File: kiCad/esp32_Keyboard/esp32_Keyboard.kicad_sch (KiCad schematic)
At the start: 171 parts, among them SW1 Switch, SW10 Switch, SW11 Switch, SW12 Switch, SW13 Switch, SW14 Switch, SW15 Switch, SW16 Switch, SW17 Switch, SW18 Switch, SW19 Switch, SW2 Switch, SW20 Switch, SW21 Switch, SW22 Switch, SW23 Switch, SW24 Switch, SW25 Switch, SW26 Switch, SW27 Switch, SW28 Switch, SW29 Switch, SW3 Switch, SW30 Switch, SW31 Switch, SW32 Switch, SW33 Switch, SW34 Switch, SW35 Switch, SW36 Switch, SW37 Switch, SW38 Switch, SW39 Switch, SW4 Switch, SW40 Switch, SW41 Switch, SW42 Switch, SW43 Switch, SW44 Switch, SW45 Switch, SW46 Switch, SW47 Switch, SW48 Switch, SW49 Switch, SW5 Switch, SW50 Switch, SW51 Switch, SW52 Switch, SW53 Switch, SW54 Switch, SW55 Switch, SW56 Switch, SW57 Switch, SW58 Switch, SW59 Switch, SW6 Switch, SW60 Switch, SW61 Switch, SW62 Switch, SW63 Switch, SW64 Switch, SW65 Switch, SW66 Switch, SW67 Switch, SW68 Switch, SW69 Switch, SW7 Switch, SW70 Switch, SW71 Switch, SW72 Switch, SW73 Switch, SW74 Switch, SW75 Switch, SW76 Switch, SW77 Switch, SW78 Switch, SW79 Switch, SW8 Switch, SW80 Switch, SW81 Switch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

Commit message: finished layout circuit baord V1
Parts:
- removed R1: 10K, ScottoKeebs_Components:Resistor_0402, symbol ScottoKeebs:Placeholder_Resistor
- added Dsp1: ~, tigmitLib:GC9A01 roundDisplay Footprint, symbol tigmitSymbolLib:GC9A01_Round_Display
- added J1, J2: Conn_01x15, Connector_PinHeader_2.54mm:PinHeader_1x15_P2.54mm_Vertical, symbol Connector_Generic:Conn_01x15
- added R2, R3, R4, R5, R6, R7: 10K, Resistor_THT:R_Axial_DIN0204_L3.6mm_D1.6mm_P7.62mm_Horizontal, symbol ScottoKeebs:Placeholder_Resistor
- added U4: ~, tigmitLib:b103 multichannel fader pot, symbol tigmitSymbolLib:b013_dual_channel_sliding_pot
- added U5: ESP32-DEVKIT-V1 DisplayHandler, ESP32-DEVKIT-V1:MODULE_ESP32_DEVKIT_V1, symbol ESP32-DEVKIT-V1:ESP32-DEVKIT-V1
- SW1, SW10, SW11, SW12, SW13, SW14, SW15, SW16, SW17, SW18, SW19, SW2, SW20, SW21, SW22, SW23, SW24, SW25, SW26, SW27, SW29, SW3, SW31, SW32, SW33, SW34, SW35, SW36, SW37, SW38, SW39, SW4, SW40, SW41, SW42, SW44, SW46, SW47, SW48, SW49, SW5, SW50, SW51, SW52, SW53, SW54, SW55, SW56, SW59, SW6, SW60, SW61, SW62, SW63, SW64, SW65, SW66, SW67, SW68, SW7, SW70, SW79, SW8, SW80, SW81, SW9: footprint ScottoKeebs_MX:MX_PCB_1.00u -> ScottoKeebs_Hotswap:Hotswap_MX_1.00u
- SW28: footprint ScottoKeebs_MX:MX_PCB_2.00u -> ScottoKeebs_Hotswap:Hotswap_MX_2.00u
- SW30, SW43: footprint ScottoKeebs_MX:MX_PCB_1.50u -> ScottoKeebs_Hotswap:Hotswap_MX_1.50u
- SW45: footprint ScottoKeebs_MX:MX_PCB_1.75u -> ScottoKeebs_Hotswap:Hotswap_MX_1.75u
- SW57, SW58: footprint ScottoKeebs_MX:MX_PCB_2.25u -> ScottoKeebs_Hotswap:Hotswap_MX_2.25u
- SW69: footprint ScottoKeebs_MX:MX_PCB_2.75u -> ScottoKeebs_Hotswap:Hotswap_MX_2.75u
- SW71, SW72, SW73, SW75, SW76, SW77, SW78: footprint ScottoKeebs_MX:MX_PCB_1.25u -> ScottoKeebs_Hotswap:Hotswap_MX_1.25u
- SW74: footprint ScottoKeebs_MX:MX_PCB_6.25u -> ScottoKeebs_Hotswap:Hotswap_MX_6.25u
- U1: value ESP32-DEVKIT-V1 -> ESP32-DEVKIT-V1 Matrix Handler
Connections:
- net GND: now also U2.13 (~{OE}), U3.13 (~{OE}), Dsp1.2 (GND), J1.2 (Pin_2), J2.14 (Pin_14), R2.2, R3.2, R4.2, R5.2, R6.2, R7.2, U4.6, U4.7 (mount), U5.2 (GND), U5.29 (GND)
- net Row0: now also U1.19 (D34), R2.1; no longer U1.21 (D32)
- net Row1: now also U1.20 (D35), R3.1; no longer U1.25 (D27)
- net Row2: now also U1.21 (D32), R4.1; no longer U1.24 (D26)
- net Row3: now also U1.22 (D33), R5.1; no longer U1.23 (D25)
- net Row4: now also U1.23 (D25), R6.1; no longer U1.15 (D23)
- net Row5: now also U1.24 (D26), R7.1; no longer U1.14 (D22)
- net VCC: now also U2.10 (~{SRCLR}), U3.10 (~{SRCLR}), Dsp1.1 (vcc), J2.15 (Pin_15), U4.3, U5.1 (3V3)
- net at U1.12 (RX0): now also J2.4 (Pin_4)
- net at U1.13 (TX0): now also J2.3 (Pin_3)
- net at U1.16 (EN): now also J1.15 (Pin_15)
- net at U1.17 (VP): now also J1.14 (Pin_14)
- net at U1.18 (VN): now also J1.13 (Pin_13)
- net at U1.26 (D14): now also J1.5 (Pin_5)
- net at U1.27 (D12): now also J1.4 (Pin_4)
- net RCLK / LATCH: now reaches U1.28 (D13)
- net RCLK / LATCH: now also U2.12 (RCLK), U3.12 (RCLK)
- net at U1.30 (VIN): now also J1.1 (Pin_1)
- net at U1.4 (D2): now also J2.12 (Pin_12)
- net at U1.5 (D4): now also J2.11 (Pin_11)
- net at U1.6 (RX2): now also J2.10 (Pin_10)
- net at U1.7 (TX2): now also J2.9 (Pin_9)
- net at U1.8 (D5): now also J2.8 (Pin_8)
- removed net RCLK: U1.10 (D19), U2.11 (SRCLK), U2.12 (RCLK), U3.11 (SRCLK), U3.12 (RCLK)
- net SER renamed SER / DATA
- net SER / DATA: now also U1.15 (D23); no longer U1.11 (D21)
- removed net /OE: U1.3 (D15), U2.13 (~{OE}), U3.13 (~{OE})
- removed net /SRCLR: U1.9 (D18), U2.10 (~{SRCLR}), U3.10 (~{SRCLR})
- new net: J1.6 (Pin_6), U1.25 (D27)
- new net: J2.6 (Pin_6), U1.10 (D19)
- new net: J2.13 (Pin_13), U1.3 (D15)
- new net DSP  SDA: Dsp1.4 (SDA), U5.15 (D23)
- new net DSP CS: Dsp1.6 (CS), J2.2 (Pin_2), U1.14 (D22), U5.14 (D22)
- new net DSP DC: Dsp1.5 (DC), U5.6 (RX2)
- new net DSP RST: Dsp1.7 (RST), U5.5 (D4)
- new net DSP SCL: Dsp1.3 (SCL), U5.9 (D18)
- new net POT slider Pin: U4.4
- new net SRCLK / CLOCK: U1.9 (D18), U2.11 (SRCLK), U3.11 (SRCLK)
- new net esp32-SDA: J2.5 (Pin_5), U1.11 (D21), U5.11 (D21)
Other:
- note removed: "for now WIP"
- note removed: "might need to pull /OE low throug 10k Res"
- moved on the sheet: U1, U2, U3

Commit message: finished PCB design
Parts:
- removed J1, J2: Conn_01x15, Connector_PinHeader_2.54mm:PinHeader_1x15_P2.54mm_Vertical, symbol Connector_Generic:Conn_01x15
- Dsp1: footprint tigmitLib:GC9A01 roundDisplay Footprint -> Connector_PinHeader_2.54mm:PinHeader_1x07_P2.54mm_Vertical
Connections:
- net POT slider Pin: now also U1.27 (D12)
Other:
- moved on the sheet: U1, U2, U3

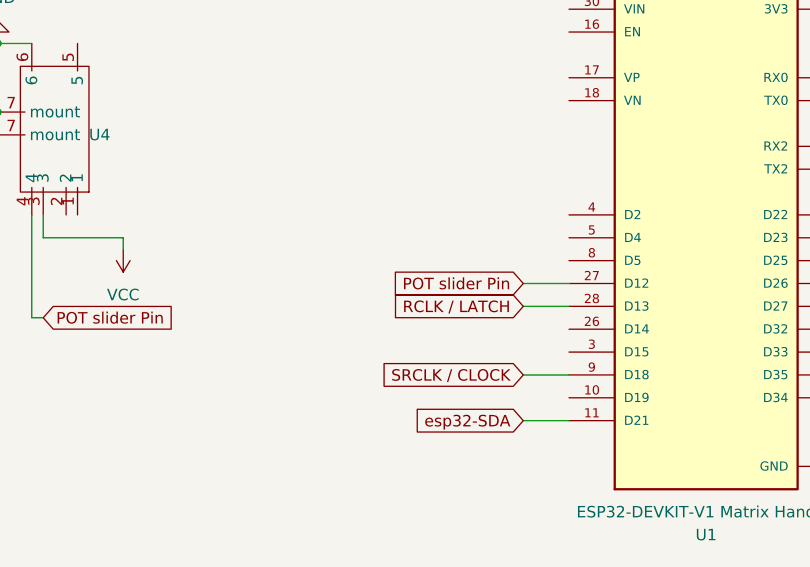
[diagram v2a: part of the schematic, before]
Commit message: display lib compiling state
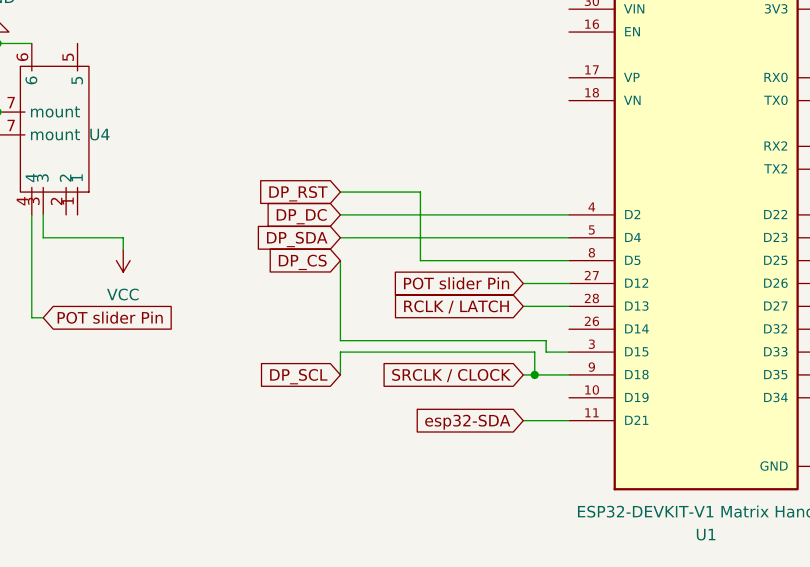
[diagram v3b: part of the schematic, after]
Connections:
- net DP_CS: now reaches U1.3 (D15)
- net DP_DC: now reaches U1.4 (D2)
- net DP_SDA: now reaches U1.5 (D4)
- net DP_RST: now reaches U1.8 (D5)
- net SRCLK / CLOCK renamed DP_SCL
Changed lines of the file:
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@@
 	)
 	(junction
+		(at -71.12 168.91)
+		(diameter 0)
+		(color 0 0 0 0)
+	)
+	(junction
 		(at 142.24 120.65)
 		(diameter 0)
@@
 	(wire
 		(pts
+			(xy -92.71 153.67) (xy -67.31 153.67)
+		)
+		(stroke
+			(width 0)
+			(type default)
+		)
+	)
+	(wire
+		(pts
 			(xy 20.32 82.55) (xy 22.86 82.55)
 		)
@@
 	(wire
 		(pts
+			(xy -92.71 148.59) (xy -83.82 148.59)
+		)
+		(stroke
+			(width 0)
+			(type default)
+		)
+	)
+	(wire
+		(pts
 			(xy 33.02 140.97) (xy 35.56 140.97)
 		)
@@
 	(wire
 		(pts
+			(xy -69.85 166.37) (xy -67.31 166.37)
+		)
+		(stroke
+			(width 0)
+			(type default)
+		)
+	)
+	(wire
+		(pts
 			(xy 311.15 93.98) (xy 314.96 93.98)
 		)
@@
 	(wire
 		(pts
+			(xy -92.71 156.21) (xy -92.71 165.1)
+		)
+		(stroke
+			(width 0)
+			(type default)
+		)
+	)
+	(wire
+		(pts
 			(xy -106.68 30.48) (xy -106.68 81.28)
 		)
@@
 	(wire
 		(pts
-			(xy -72.39 168.91) (xy -67.31 168.91)
+			(xy -72.39 168.91) (xy -71.12 168.91)
 		)
 		(stroke
@@
 	(wire
 		(pts
+			(xy -92.71 151.13) (xy -67.31 151.13)
+		)
+		(stroke
+			(width 0)
+			(type default)
+		)
+	)
+	(wire
+		(pts
 			(xy -62.23 16.51) (xy -120.65 16.51)
 		)
@@
 	(wire
 		(pts
+			(xy -71.12 166.37) (xy -71.12 168.91)
+		)
+		(stroke
+			(width 0)
+			(type default)
+		)
+	)
+	(wire
+		(pts
 			(xy 109.22 100.33) (xy 111.76 100.33)
 		)
@@
 	(wire
 		(pts
+			(xy -92.71 168.91) (xy -92.71 166.37)
+		)
+		(stroke
+			(width 0)
+			(type default)
+		)
+	)
+	(wire
+		(pts
 			(xy 334.7998 36.2996) (xy 334.5436 36.2996)
 		)
@@
 	(wire
 		(pts
+			(xy -71.12 168.91) (xy -67.31 168.91)
+		)
+		(stroke
+			(width 0)
+			(type default)
+		)
+	)
+	(wire
+		(pts
 			(xy 81.28 59.69) (xy 81.28 80.01)
 		)
@@
 	(wire
 		(pts
+			(xy -83.82 148.59) (xy -83.82 156.21)
+		)
+		(stroke
+			(width 0)
+			(type default)
+		)
+	)
+	(wire
+		(pts
 			(xy 190.5 19.05) (xy 190.5 29.21)
 		)
@@
 	(wire
 		(pts
+			(xy -69.85 165.1) (xy -69.85 166.37)
+		)
+		(stroke
+			(width 0)
+			(type default)
+		)
+	)
+	(wire
+		(pts
 			(xy 160.02 82.55) (xy 175.26 82.55)
 		)
@@
 	(wire
 		(pts
+			(xy -92.71 166.37) (xy -71.12 166.37)
+		)
+		(stroke
+			(width 0)
+			(type default)
+		)
+	)
+	(wire
+		(pts
 			(xy 311.15 116.84) (xy 313.69 116.84)
 		)
@@
 	(wire
 		(pts
+			(xy -83.82 156.21) (xy -67.31 156.21)
+		)
+		(stroke
+			(width 0)
+			(type default)
+		)
+	)
+	(wire
+		(pts
 			(xy -59.69 48.26) (xy -59.69 64.77)
 		)
@@
 	(wire
 		(pts
+			(xy -92.71 165.1) (xy -69.85 165.1)
+		)
+		(stroke
+			(width 0)
+			(type default)
+		)
+	)
+	(wire
+		(pts
 			(xy 349.25 73.66) (xy 345.44 73.66)
 		)
@@
 		)
 	)
+	(global_label "DP_CS"
+		(shape input)
+		(at -92.71 156.21 180)
+		(fields_autoplaced yes)
+		(effects
+			(font
+				(size 1.27 1.27)
+			)
+			(justify right)
+		)
+		(property "Intersheetrefs" "${INTERSHEET_REFS}"
+			(at -101.6823 156.21 0)
+			(effects
+				(font
+					(size 1.27 1.27)
+				)
+				(justify right)
+				(hide yes)
+			)
+		)
+	)
 	(global_label "Col1"
 		(shape input)
@@
 		)
 	)
+	(global_label "DP_SDA"
+		(shape input)
+		(at -92.71 153.67 180)
+		(fields_autoplaced yes)
+		(effects
+			(font
+				(size 1.27 1.27)
+			)
+			(justify right)
+		)
+		(property "Intersheetrefs" "${INTERSHEET_REFS}"
+			(at -102.7709 153.67 0)
+			(effects
+				(font
+					(size 1.27 1.27)
+				)
+				(justify right)
+				(hide yes)
+			)
+		)
+	)
 	(global_label "Row5"
 		(shape input)
@@
 		)
 	)
+	(global_label "DP_DC"
+		(shape input)
+		(at -92.71 151.13 180)
+		(fields_autoplaced yes)
+		(effects
+			(font
+				(size 1.27 1.27)
+			)
+			(justify right)
+		)
+		(property "Intersheetrefs" "${INTERSHEET_REFS}"
+			(at -101.7428 151.13 0)
+			(effects
+				(font
+					(size 1.27 1.27)
+				)
+				(justify right)
+				(hide yes)
+			)
+		)
+	)
 	(global_label "Col11"
 		(shape input)
@@
 		)
 	)
+	(global_label "DP_RST"
+		(shape input)
+		(at -92.71 148.59 180)
+		(fields_autoplaced yes)
+		(effects
+			(font
+				(size 1.27 1.27)
+			)
+			(justify right)
+		)
+		(property "Intersheetrefs" "${INTERSHEET_REFS}"
+			(at -102.6499 148.59 0)
+			(effects
+				(font
+					(size 1.27 1.27)
+				)
+				(justify right)
+				(hide yes)
+			)
+		)
+	)
 	(global_label "Col15"
 		(shape input)
@@
 			(effects
 				(font
+					(size 1.27 1.27)
+				)
+				(justify right)
+				(hide yes)
+			)
+		)
+	)
+	(global_label "DP_SCL"
+		(shape input)
+		(at -92.71 168.91 180)
+		(fields_autoplaced yes)
+		(effects
+			(font
+				(size 1.27 1.27)
+			)
+			(justify right)
+		)
+		(property "Intersheetrefs" "${INTERSHEET_REFS}"
+			(at -102.7104 168.91 0)
+			(effects
+				(font

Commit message: commit current work
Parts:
- removed S1: stab L shift 2.25u, PCM_marbastlib-mx:STAB_MX_2.25u, symbol PCM_marbastlib-mx:MX_stab
- removed U5: ESP32-DEVKIT-V1 DisplayHandler, ESP32-DEVKIT-V1:MODULE_ESP32_DEVKIT_V1, symbol ESP32-DEVKIT-V1:ESP32-DEVKIT-V1
- added BT1: Battery_Cell, tigmitLib:battery solder pins, symbol Device:Battery_Cell
- added C1: 100µF, Capacitor_THT:CP_Radial_D10.0mm_P2.50mm, symbol Device:C_Polarized
- added C2: 100nF, Capacitor_THT:C_Rect_L7.0mm_W2.5mm_P5.00mm, symbol Device:C
- added R1: 4k7, Resistor_THT:R_Axial_DIN0204_L3.6mm_D1.6mm_P7.62mm_Horizontal, symbol ScottoKeebs:Placeholder_Resistor
- added R10, R9: 100k, Resistor_THT:R_Axial_DIN0204_L3.6mm_D1.6mm_P7.62mm_Horizontal, symbol ScottoKeebs:Placeholder_Resistor
- added R8: 10k, Resistor_THT:R_Axial_DIN0204_L3.6mm_D1.6mm_P7.62mm_Horizontal, symbol ScottoKeebs:Placeholder_Resistor
- added S5: stab 2u, PCM_marbastlib-mx:STAB_MX_2u, symbol PCM_marbastlib-mx:MX_stab
- added U5: ~, tp4056:TP4056-18650, symbol tigmitSymbolLib:tp_lipo_chargin_module
- added U6: SK12D07VG4, SK12D07VG4:SK12D07VG4, symbol SK12D07VG4:SK12D07VG4
- added mcp1: ~, tigmitLib:MCP1700 3.3V, symbol tigmitSymbolLib:tim_mcp1700-3302e
- S2: renamed from S5; value stab backspace 2u -> stab 2u
- S3: value stab R shift 2.75u -> stab 2u; footprint PCM_marbastlib-mx:STAB_MX_2.75u -> PCM_marbastlib-mx:STAB_MX_2u
- S4: value stab enter 2.25u -> stab 2u; footprint PCM_marbastlib-mx:STAB_MX_2.25u -> PCM_marbastlib-mx:STAB_MX_2u
- U1: footprint ESP32-DEVKIT-V1:MODULE_ESP32_DEVKIT_V1 -> tigmitLib:ESP32 Vroom Devkit V1
- U2, U3: footprint SN74HC595NG4:DIP794W45P254L1969H508Q16 -> tigmitLib:SNH Shift register
- renumbered S2 to S1
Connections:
- net DSP  SDA is gone; now on net DP_SDA: Dsp1.4 (SDA)
- net DSP DC is gone; now on net DP_DC: Dsp1.5 (DC)
- net DSP RST is gone; now on net DP_RST: Dsp1.7 (RST)
- net DSP SCL is gone; now on net DP_SCL: Dsp1.3 (SCL)
- net DP_CS: now also Dsp1.6 (CS)
- net GND: now also C1.2, C2.2, R8.1, R9.1, U5.2 (GND), U5.4 (OUT-), mcp1.2 (gnd)
- net VCC: now also C1.1, C2.1, mcp1.3 (3.3_out)
- net batt_voltage_Pin: now reaches U1.25 (D27)
- net batt_voltage_Pin: now also R10.1, R9.2
- net batt_chargesense: now reaches U1.26 (D14)
- net batt_chargesense: now also R1.2, R8.2
- net DSP CS renamed esp32-SCL
- net esp32-SCL: no longer Dsp1.6 (CS)
- new net: R10.2, U5.3 (OUT+), mcp1.1 (Vin)
- new net: R1.1, U5.1 (ind)
- new net: U5.5 (B+), U6.2
- new net Battery+: BT1.1 (+), U6.COM
- new net Battery-: BT1.2 (-), U5.6 (B-)
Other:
- moved on the sheet: S1, S2, U1, U4
